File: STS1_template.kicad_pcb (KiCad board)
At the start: 4 copper layers, 85 x 85 mm, 24 parts, among them CON1 DISCO-CON1, CON11 DISCO-CON1, CON2 DISCO-CON2, CON21 DISCO-CON2, IC1 W25Q01JVZEIQ, IC2 CY15B108QN-40SXI, IC3 STM32F411RET6TR, J1 Conn_01x02_Female, J2 Conn_02x16_Odd_Even, J3 Conn_01x02_Female, J4 Conn_02x16_Odd_Even, J5 Conn_02x16_Odd_Even, J6 Conn_02x16_Odd_Even, U1 coordinate_system

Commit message: new template
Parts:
- removed IC3: STM32F411RET6TR, STM32F411RET6TR:QFP50P1200X1200X160-64N
- added C1: 20p, Capacitor_SMD:C_0805_2012Metric, F.Cu at (236.4, 93.4)
- added C10: 100n, Capacitor_SMD:C_0805_2012Metric, F.Cu at (240.9, 93.4)
- added C11: 100n, Capacitor_SMD:C_0805_2012Metric, F.Cu at (209.6, 109.2)
- added C12: 47u, Capacitor_SMD:C_0805_2012Metric, F.Cu at (223.0, 103.7)
- added C13: 100n, Capacitor_SMD:C_0805_2012Metric, F.Cu at (281.3, 76.1)
- added C14: 47u, Capacitor_SMD:C_0805_2012Metric, F.Cu at (276.8, 79.1)
- added C15: 100n, Capacitor_SMD:C_0805_2012Metric, F.Cu at (276.8, 76.1)
- added C16: 47u, Capacitor_SMD:C_0805_2012Metric, F.Cu at (281.3, 79.1)
- added C2: 20p, Capacitor_SMD:C_0805_2012Metric, F.Cu at (263.2, 60.8)
- added C3: 1u, Capacitor_SMD:C_0805_2012Metric, F.Cu at (250.9, 84.1)
- added C4: 100n, Capacitor_SMD:C_0805_2012Metric, F.Cu at (268.8, 69.9)
- added C5: 100n, Capacitor_SMD:C_0805_2012Metric, F.Cu at (264.3, 72.9)
- added C6: 4.7u, Capacitor_SMD:C_0805_2012Metric, F.Cu at (267.7, 66.9)
- added C7: 100n, Capacitor_SMD:C_0805_2012Metric, F.Cu at (264.3, 69.9)
- added C8: 4.7u, Capacitor_SMD:C_0805_2012Metric, F.Cu at (263.2, 66.9)
- added C9: 100n, Capacitor_SMD:C_0805_2012Metric, F.Cu at (267.7, 63.8)
- added D1: LED, LED_SMD:LED_0805_2012Metric, F.Cu at (267.7, 60.8)
- added D2: LED, LED_SMD:LED_0805_2012Metric, F.Cu at (263.2, 63.8)
- added D3: LED, LED_SMD:LED_0805_2012Metric, F.Cu at (214.1, 109.2)
- added FLASH1: W25Q01JVZEIQ, W25Q01JVZEIQ:SON127P800X600X80-9N-D, F.Cu at (180.9, 64.8)
- added FRAM1: CY15B108QN-40SXI, CY15B108QN-40SXI:SOIC127P800X203-8N, F.Cu at (180.9, 56.8)
- added J10: Conn_01x01_Male, Connector_PinHeader_2.54mm:PinHeader_1x01_P2.54mm_Vertical, F.Cu at (237.6, 84.9)
- added J11: Conn_01x01_Male, Connector_PinHeader_2.54mm:PinHeader_1x01_P2.54mm_Vertical, F.Cu at (251.0, 70.9)
- added J12: Conn_01x01_Male, Connector_PinHeader_2.54mm:PinHeader_1x01_P2.54mm_Vertical, F.Cu at (249.9, 89.5)
- added J13: Conn_01x01_Male, Connector_PinHeader_2.54mm:PinHeader_1x01_P2.54mm_Vertical, F.Cu at (251.0, 80.2)
- added J14: Conn_01x01_Male, Connector_PinHeader_2.54mm:PinHeader_1x01_P2.54mm_Vertical, F.Cu at (237.6, 70.9)
- added J15: Conn_01x01_Male, Connector_PinHeader_2.54mm:PinHeader_1x01_P2.54mm_Vertical, F.Cu at (223.1, 66.3)
- added J16: Conn_01x01_Male, Connector_PinHeader_2.54mm:PinHeader_1x01_P2.54mm_Vertical, F.Cu at (224.2, 84.9)
- added J17: Conn_01x01_Male, Connector_PinHeader_2.54mm:PinHeader_1x01_P2.54mm_Vertical, F.Cu at (223.1, 90.9)
- added J18: Conn_01x01_Male, Connector_PinHeader_2.54mm:PinHeader_1x01_P2.54mm_Vertical, F.Cu at (236.5, 66.3)
- added J19: Conn_01x01_Male, Connector_PinHeader_2.54mm:PinHeader_1x01_P2.54mm_Vertical, F.Cu at (224.2, 80.2)
- added J20: Conn_01x01_Male, Connector_PinHeader_2.54mm:PinHeader_1x01_P2.54mm_Vertical, F.Cu at (224.2, 75.6)
- added J21: Conn_01x01_Male, Connector_PinHeader_2.54mm:PinHeader_1x01_P2.54mm_Vertical, F.Cu at (224.2, 70.9)
- added J22: Conn_01x01_Male, Connector_PinHeader_2.54mm:PinHeader_1x01_P2.54mm_Vertical, F.Cu at (223.1, 61.6)
- added J23: Conn_01x01_Male, Connector_PinHeader_2.54mm:PinHeader_1x01_P2.54mm_Vertical, F.Cu at (236.5, 61.6)
- added J24: Conn_01x01_Male, Connector_PinHeader_2.54mm:PinHeader_1x01_P2.54mm_Vertical, F.Cu at (209.7, 105.4)
- added J25: Conn_01x01_Male, Connector_PinHeader_2.54mm:PinHeader_1x01_P2.54mm_Vertical, F.Cu at (209.7, 100.7)
- added J7: Conn_01x01_Male, Connector_PinHeader_2.54mm:PinHeader_1x01_P2.54mm_Vertical, F.Cu at (237.6, 80.2)
- added J8: Conn_01x01_Male, Connector_PinHeader_2.54mm:PinHeader_1x01_P2.54mm_Vertical, F.Cu at (236.5, 89.5)
- added J9: Conn_01x01_Male, Connector_PinHeader_2.54mm:PinHeader_1x01_P2.54mm_Vertical, F.Cu at (251.0, 75.6)
- added R1: 220, Resistor_SMD:R_0805_2012Metric, F.Cu at (249.7, 93.3)
- added R2: 100, Resistor_SMD:R_0805_2012Metric, F.Cu at (264.3, 75.9)
- added R3: 100, Resistor_SMD:R_0805_2012Metric, F.Cu at (245.3, 93.3)
- added R4: 4k7, Resistor_SMD:R_0805_2012Metric, F.Cu at (227.7, 99.9)
- added R5: 100, Resistor_SMD:R_0805_2012Metric, F.Cu at (223.0, 106.7)
- IC1: value W25Q01JVZEIQ -> STM32F411RET6TR; footprint W25Q01JVZEIQ:SON127P800X600X80-9N-D -> STM32F411RET6TR:QFP50P1200X1200X160-64N
- IC2: value CY15B108QN-40SXI -> STWD100PYW83F; footprint CY15B108QN-40SXI:SOIC127P800X203-8N -> SamacSys_Parts:SOT65P210X110-5N
- J1: footprint Connector_PinSocket_2.00mm:PinSocket_1x02_P2.00mm_Vertical -> Connector_PinHeader_2.54mm:PinHeader_1x02_P2.54mm_Vertical
- J2: value Conn_02x16_Odd_Even -> Conn_01x05_Female; footprint Connector_PinHeader_2.00mm:PinHeader_2x16_P2.00mm_Vertical_SMD -> Connector_PinHeader_2.54mm:PinHeader_1x05_P2.54mm_Horizontal
- J3: value Conn_01x02_Female -> Conn_01x01_Male; footprint Connector_PinSocket_2.00mm:PinSocket_1x02_P2.00mm_Vertical -> Connector_PinHeader_2.54mm:PinHeader_1x01_P2.54mm_Vertical
- J4, J5, J6: value Conn_02x16_Odd_Even -> Conn_01x01_Male; footprint Connector_PinHeader_2.00mm:PinHeader_2x16_P2.00mm_Vertical_SMD -> Connector_PinHeader_2.54mm:PinHeader_1x01_P2.54mm_Vertical
- moved J3 92.9 mm to (209.7, 90.9)
- moved J4 91.8 mm to (249.9, 61.6), turned to 0 degrees
- moved J5 86.4 mm to (237.6, 75.6), turned to 0 degrees
- moved IC2 67.8 mm to (223.1, 100.3), turned to 0 degrees
- moved J6 67.7 mm to (249.9, 66.3)
- moved J1 67.6 mm to (236.0, 100.3)
- moved J2 43.0 mm to (152.9, 43.8), turned to 90 degrees
- moved IC1 30.6 mm to (156.9, 83.8), turned to 0 degrees
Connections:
- net Earth renamed Net-(IC1-Pad4)
- IC1 pad 1: Net-(IC1-Pad1) -> /STS1_RF/LoRa_VCC
- IC1 pad 5: Net-(IC1-Pad5) -> Net-(C1-Pad2)
- IC1 pad 7: Net-(IC1-Pad7) -> /STS1_COBC_uC/STM32_NRST
- IC1 pad 8: +3V3 -> Net-(IC1-Pad8)
- IC2 pad 2: Net-(IC2-Pad2) -> GND
- IC2 pad 3: Net-(IC2-Pad3) -> GND
- IC2 pad 4: Net-(IC2-Pad4) -> /STS1_COBC_uC/STM32_PA9(Watchdog_toggle)
- IC2 pad 5: Net-(IC2-Pad5) -> /STS1_RF/LoRa_VCC
- J1 pad 1: Net-(J1-Pad1) -> GND
- J1 pad 2: Net-(J1-Pad2) -> /STS1_RF/LoRa_VCC
- J2 pad 1: Net-(J2-Pad1) -> /STS1_RF/LoRa_VCC
- J2 pad 2: Net-(IC3-Pad1) -> Net-(IC1-Pad49)
- J2 pad 3: Net-(J2-Pad3) -> GND
- J2 pad 4: Net-(IC3-Pad2) -> Net-(IC1-Pad46)
- J2 pad 5: Net-(J2-Pad5) -> /STS1_COBC_uC/STM32_NRST
- J3 pad 1: Net-(J3-Pad1) -> /STS1_RF/LoRa_NSS
- J4 pad 1: Net-(IC3-Pad64) -> /STS1_RF/RF4463_SDI
- J5 pad 1: Net-(J5-Pad1) -> /STS1_COBC_Memories/FRAM_DataOutput
- J6 pad 1: Net-(IC3-Pad48) -> /STS1_COBC_Memories/FRAM_DataInput
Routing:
- net Net-(IC1-Pad6): track 115.8 -> 0.00 mm
- net +3V3: track 86.2 -> 0.00 mm, vias 4 -> 5
- net Net-(IC2-Pad2): track 49.0 -> 0.00 mm
- net Net-(IC3-Pad17): track 23.4 -> 0.00 mm
- net Net-(IC3-Pad33): track 23.2 -> 0.00 mm
- net Net-(IC3-Pad32): track 23.2 -> 0.00 mm
- net Net-(IC3-Pad48): track 22.9 -> 0.00 mm
- net Net-(IC3-Pad35): track 22.8 -> 0.00 mm
- net Net-(IC3-Pad18): track 22.7 -> 0.00 mm
- net Net-(IC3-Pad34): track 22.6 -> 0.00 mm
- net Net-(IC3-Pad31): track 22.6 -> 0.00 mm
- net Net-(IC3-Pad47): track 22.4 -> 0.00 mm
- net Net-(IC3-Pad19): track 22.1 -> 0.00 mm
- net Net-(IC3-Pad30): track 22.0 -> 0.00 mm
- net Net-(IC3-Pad46): track 21.6 -> 0.00 mm
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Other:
- board text added: "TU Wien Space Team STS [STS1 COBC Prototype] v1.0"
- board text removed: "TU Wien Space Team STS1 [COBC] [V1]"

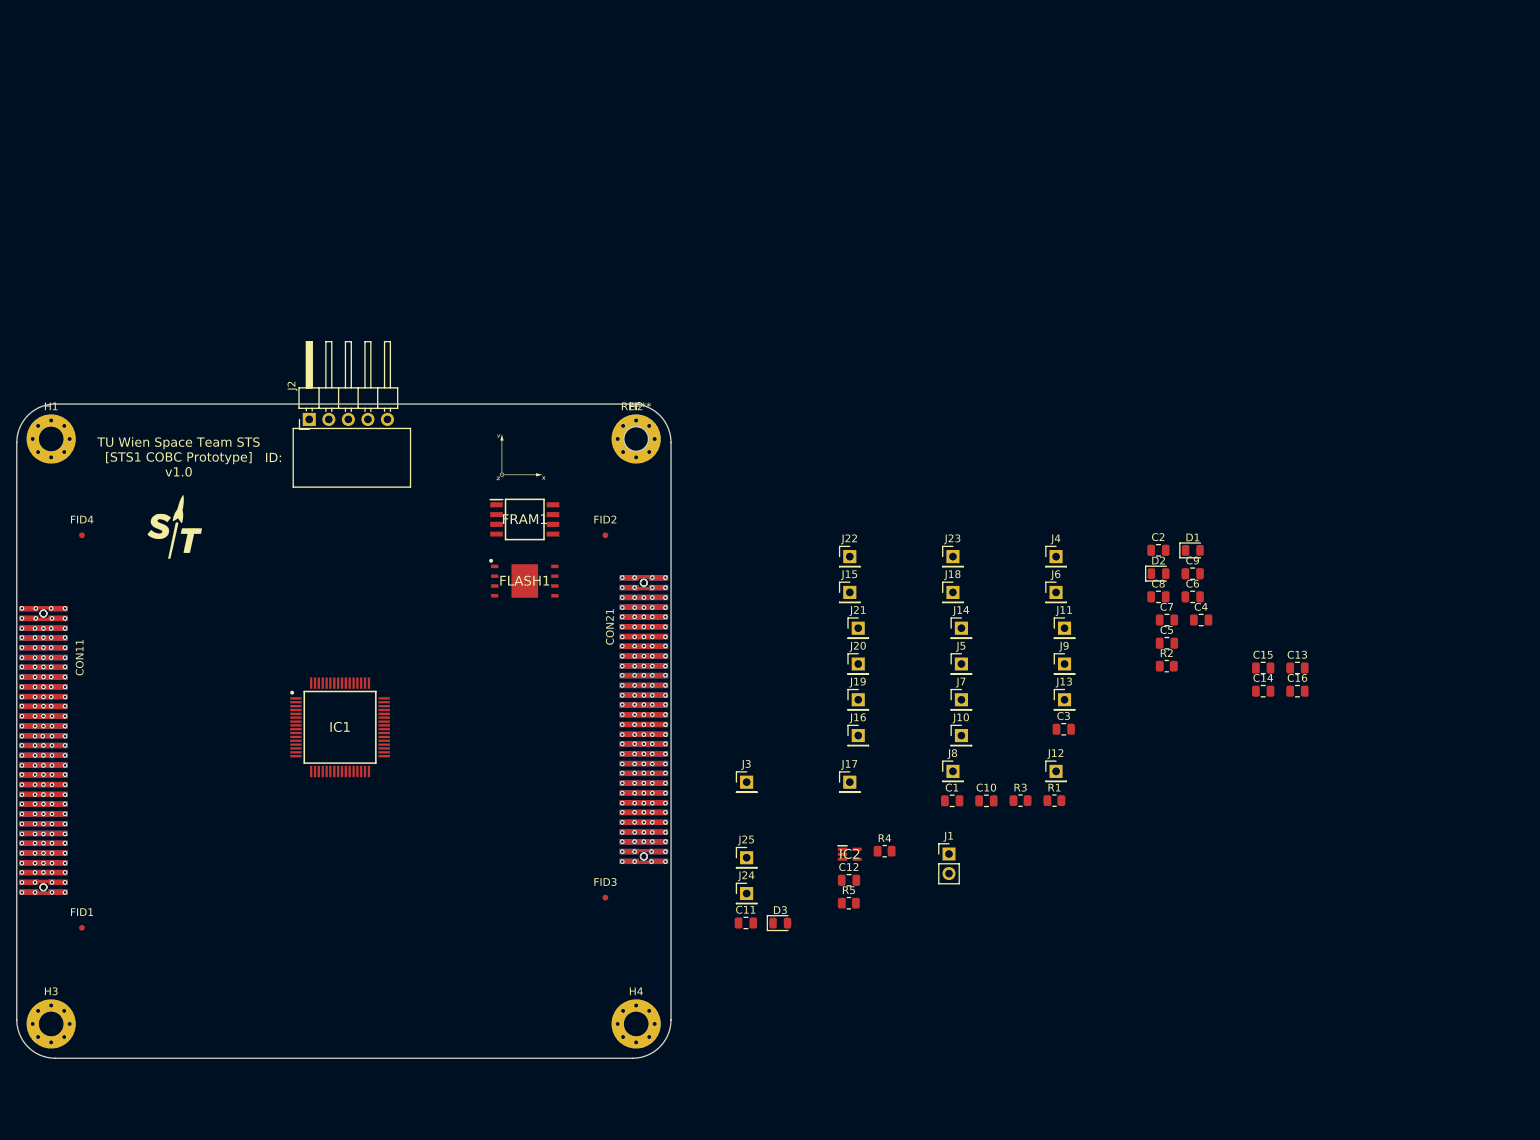
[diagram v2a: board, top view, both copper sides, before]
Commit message: Issues removed + further layout development
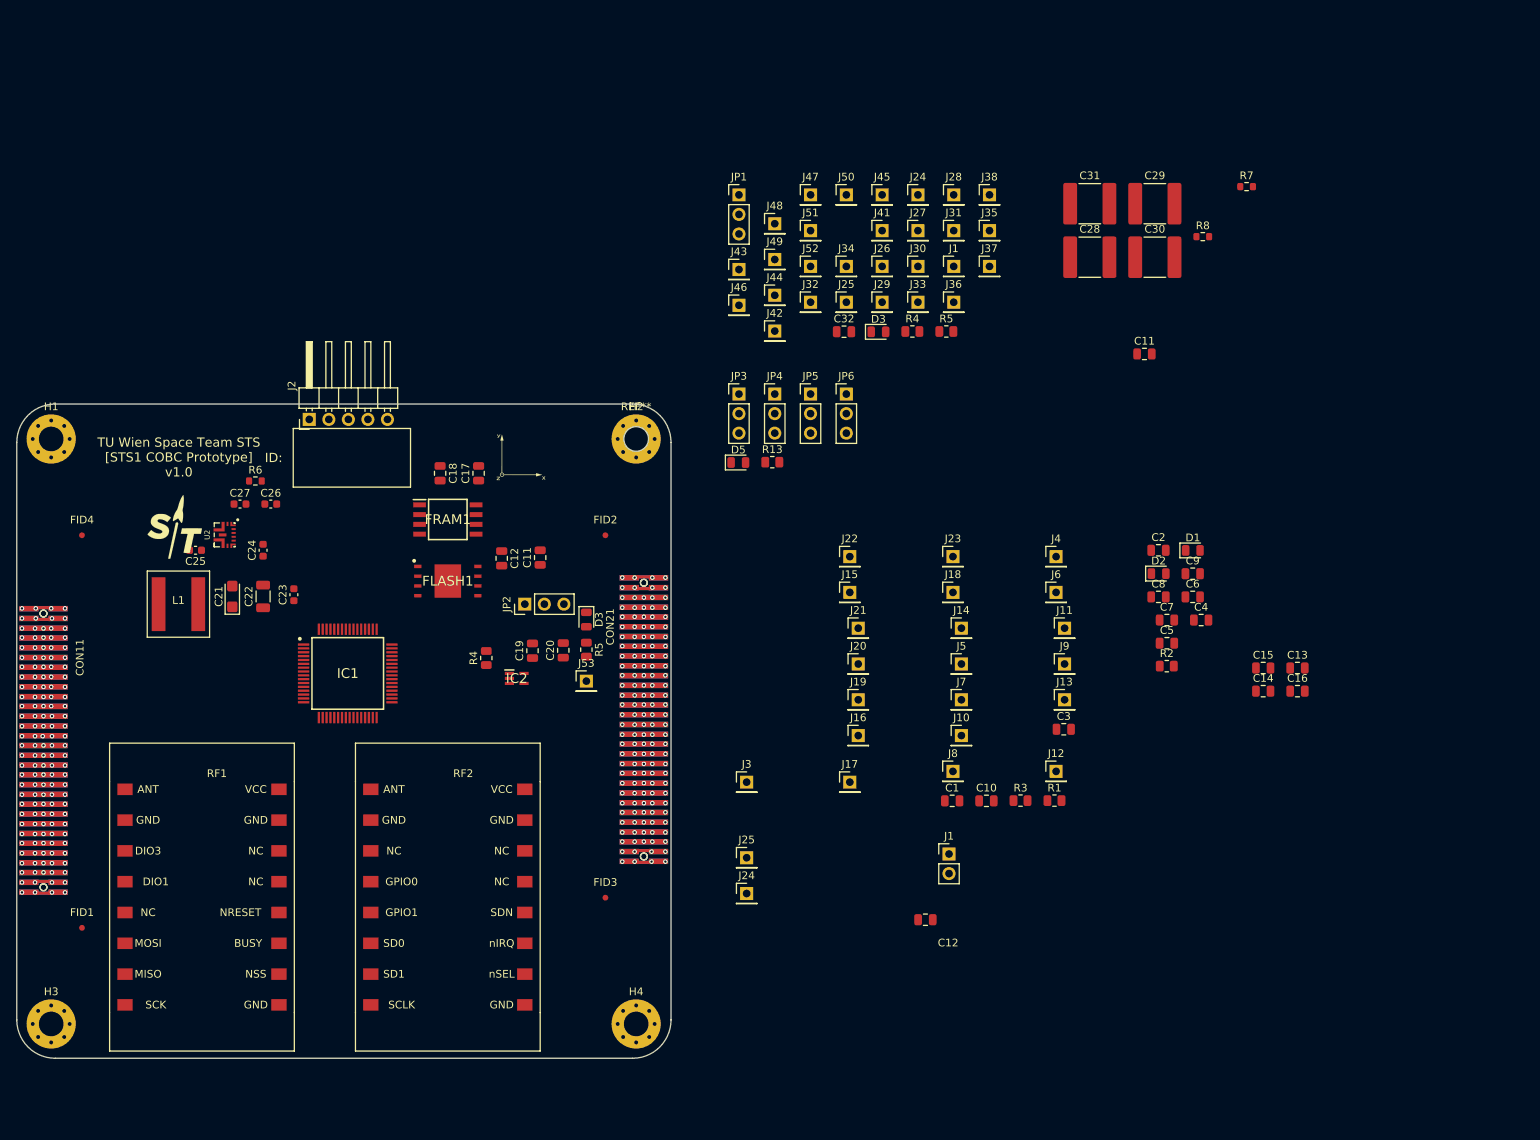
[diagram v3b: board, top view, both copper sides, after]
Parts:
- added C11: 100n, Capacitor_SMD:C_0805_2012Metric, F.Cu at (261.4, 35.3)
- added C12: 47u, Capacitor_SMD:C_0805_2012Metric, F.Cu at (177.9, 61.9)
- added C17: 100n, Capacitor_SMD:C_0805_2012Metric, F.Cu at (174.9, 50.8)
- added C18: 47u, Capacitor_SMD:C_0805_2012Metric, F.Cu at (169.9, 50.8)
- added C19: 100n, Capacitor_SMD:C_0805_2012Metric, F.Cu at (181.9, 73.8)
- added C20: 47u, Capacitor_SMD:C_0805_2012Metric, F.Cu at (185.9, 73.8)
- added C21: 47uF, Capacitor_Tantalum_SMD:CP_EIA-3216-18_Kemet-A, F.Cu at (142.9, 66.8)
- added C22: 10uF, Capacitor_SMD:C_1206_3216Metric, F.Cu at (146.9, 66.8)
- added C23: 100nF, Capacitor_SMD:C_0603_1608Metric, F.Cu at (150.9, 66.6)
- added C24: 150nF, Capacitor_SMD:C_0603_1608Metric, F.Cu at (146.9, 60.8)
- added C25: 2.2uF, Capacitor_SMD:C_0603_1608Metric, F.Cu at (138.1, 60.8)
- added C26: 39nF, Capacitor_SMD:C_0603_1608Metric, F.Cu at (147.9, 54.8)
- added C27: 82pF, Capacitor_SMD:C_0603_1608Metric, F.Cu at (143.9, 54.8)
- added C28: 68uF, Capacitor_SMD:C_2220_5650Metric, F.Cu at (254.3, 22.7)
- added C29: 68uF, Capacitor_SMD:C_2220_5650Metric, F.Cu at (262.8, 15.8)
- added C30: 68uF, Capacitor_SMD:C_2220_5650Metric, F.Cu at (262.8, 22.7)
- added C31: 68uF, Capacitor_SMD:C_2220_5650Metric, F.Cu at (254.3, 15.8)
- added C32: 100n, Capacitor_SMD:C_0805_2012Metric, F.Cu at (222.4, 32.4)
- added D3: LED, LED_SMD:LED_0805_2012Metric, F.Cu at (226.8, 32.4)
- added D5: LED, LED_SMD:LED_0805_2012Metric, F.Cu at (208.6, 49.4)
- added J1: Conn_01x01_Male, Connector_PinHeader_2.54mm:PinHeader_1x01_P2.54mm_Vertical, F.Cu at (236.6, 23.9)
- added J24: Conn_01x01_Male, Connector_PinHeader_2.54mm:PinHeader_1x01_P2.54mm_Vertical, F.Cu at (232.0, 14.6)
- added J25: Conn_01x01_Male, Connector_PinHeader_2.54mm:PinHeader_1x01_P2.54mm_Vertical, F.Cu at (222.7, 28.6)
- added J26: Conn_01x01_Male, Connector_PinHeader_2.54mm:PinHeader_1x01_P2.54mm_Vertical, F.Cu at (227.3, 23.9)
- added J27: Conn_01x01_Male, Connector_PinHeader_2.54mm:PinHeader_1x01_P2.54mm_Vertical, F.Cu at (232.0, 19.3)
- added J28: Conn_01x01_Male, Connector_PinHeader_2.54mm:PinHeader_1x01_P2.54mm_Vertical, F.Cu at (236.6, 14.6)
- added J29: Conn_01x01_Male, Connector_PinHeader_2.54mm:PinHeader_1x01_P2.54mm_Vertical, F.Cu at (227.3, 28.6)
- added J30: Conn_01x01_Male, Connector_PinHeader_2.54mm:PinHeader_1x01_P2.54mm_Vertical, F.Cu at (232.0, 23.9)
- added J31: Conn_01x01_Male, Connector_PinHeader_2.54mm:PinHeader_1x01_P2.54mm_Vertical, F.Cu at (236.6, 19.3)
- added J32: Conn_01x01_Male, Connector_PinHeader_2.54mm:PinHeader_1x01_P2.54mm_Vertical, F.Cu at (218.0, 28.6)
- added J33: Conn_01x01_Male, Connector_PinHeader_2.54mm:PinHeader_1x01_P2.54mm_Vertical, F.Cu at (232.0, 28.6)
- added J34: Conn_01x01_Male, Connector_PinHeader_2.54mm:PinHeader_1x01_P2.54mm_Vertical, F.Cu at (222.7, 23.9)
- added J35: Conn_01x01_Male, Connector_PinHeader_2.54mm:PinHeader_1x01_P2.54mm_Vertical, F.Cu at (241.3, 19.3)
- added J36: Conn_01x01_Male, Connector_PinHeader_2.54mm:PinHeader_1x01_P2.54mm_Vertical, F.Cu at (236.6, 28.6)
- added J37: Conn_01x01_Male, Connector_PinHeader_2.54mm:PinHeader_1x01_P2.54mm_Vertical, F.Cu at (241.3, 23.9)
- added J38: Conn_01x01_Male, Connector_PinHeader_2.54mm:PinHeader_1x01_P2.54mm_Vertical, F.Cu at (241.3, 14.6)
- added J41: Conn_01x01_Male, Connector_PinHeader_2.54mm:PinHeader_1x01_P2.54mm_Vertical, F.Cu at (227.3, 19.3)
- added J42: Conn_01x01_Male, Connector_PinHeader_2.54mm:PinHeader_1x01_P2.54mm_Vertical, F.Cu at (213.4, 32.3)
- added J43: Conn_01x01_Male, Connector_PinHeader_2.54mm:PinHeader_1x01_P2.54mm_Vertical, F.Cu at (208.7, 24.3)
- added J44: Conn_01x01_Male, Connector_PinHeader_2.54mm:PinHeader_1x01_P2.54mm_Vertical, F.Cu at (213.4, 27.7)
- added J45: Conn_01x01_Male, Connector_PinHeader_2.54mm:PinHeader_1x01_P2.54mm_Vertical, F.Cu at (227.3, 14.6)
- added J46: Conn_01x01_Male, Connector_PinHeader_2.54mm:PinHeader_1x01_P2.54mm_Vertical, F.Cu at (208.7, 29.0)
- added J47: Conn_01x01_Male, Connector_PinHeader_2.54mm:PinHeader_1x01_P2.54mm_Vertical, F.Cu at (218.0, 14.6)
- added J48: Conn_01x01_Male, Connector_PinHeader_2.54mm:PinHeader_1x01_P2.54mm_Vertical, F.Cu at (213.4, 18.4)
- added J49: Conn_01x01_Male, Connector_PinHeader_2.54mm:PinHeader_1x01_P2.54mm_Vertical, F.Cu at (213.4, 23.0)
- added J50: Conn_01x01_Male, Connector_PinHeader_2.54mm:PinHeader_1x01_P2.54mm_Vertical, F.Cu at (222.7, 14.6)
- added J51: Conn_01x01_Male, Connector_PinHeader_2.54mm:PinHeader_1x01_P2.54mm_Vertical, F.Cu at (218.0, 19.3)
- added J52: Conn_01x01_Male, Connector_PinHeader_2.54mm:PinHeader_1x01_P2.54mm_Vertical, F.Cu at (218.0, 23.9)
- added J53: Conn_01x01_Male, Connector_PinHeader_2.54mm:PinHeader_1x01_P2.54mm_Vertical, F.Cu at (188.9, 77.8)
- added JP1: Jumper_NC_Dual, Connector_PinHeader_2.54mm:PinHeader_1x03_P2.54mm_Vertical, F.Cu at (208.7, 14.6)
- added JP2: Jumper_NC_Dual, Connector_PinHeader_2.54mm:PinHeader_1x03_P2.54mm_Vertical, F.Cu at (180.9, 67.8)
- added JP3: Jumper_NC_Dual, Connector_PinHeader_2.54mm:PinHeader_1x03_P2.54mm_Vertical, F.Cu at (208.7, 40.5)
- added JP4: Jumper_NC_Dual, Connector_PinHeader_2.54mm:PinHeader_1x03_P2.54mm_Vertical, F.Cu at (213.4, 40.5)
- added JP5: Jumper_NC_Dual, Connector_PinHeader_2.54mm:PinHeader_1x03_P2.54mm_Vertical, F.Cu at (218.0, 40.5)
- added JP6: Jumper_NC_Dual, Connector_PinHeader_2.54mm:PinHeader_1x03_P2.54mm_Vertical, F.Cu at (222.7, 40.5)
- added L1: 1uH, STS1_DCDC:XAL8080, F.Cu at (135.9, 67.8)
- added R13: 15, Resistor_SMD:R_0805_2012Metric, F.Cu at (213.1, 49.4)
- added R4: 4k7, Resistor_SMD:R_0805_2012Metric, F.Cu at (231.3, 32.4)
- added R5: 100, Resistor_SMD:R_0805_2012Metric, F.Cu at (235.7, 32.4)
- added R6: 48k7, Resistor_SMD:R_0603_1608Metric, F.Cu at (145.9, 51.8)
- added R7: 357k, Resistor_SMD:R_0603_1608Metric, F.Cu at (274.7, 13.6)
- added R8: 48k7, Resistor_SMD:R_0603_1608Metric, F.Cu at (269.0, 20.1)
- added RF1: LoRa1268F30, STS1_RF:LoRa1268F30, F.Cu at (149.0, 91.9)
- added RF2: RF4463F30, STS1_RF:STS1_RF4463F30, F.Cu at (180.9, 91.9)
- added U2: TPS61288, STS1_DCDC:VQFN-HR, F.Cu at (141.9, 58.8)
- moved R4 57.5 mm to (175.9, 74.8), turned to 90 degrees
- moved C11 54.5 mm to (182.9, 61.8), turned to 90 degrees
- moved IC2 48.9 mm to (179.8, 77.5)
- moved R5 47.4 mm to (188.9, 73.7), turned to 270 degrees
- moved D3 46.8 mm to (188.9, 69.8), turned to 270 degrees
- moved C12 11.2 mm to (232.9, 108.8)
- moved FLASH1 10.0 mm to (170.9, 64.8)
- moved FRAM1 10.0 mm to (170.9, 56.8)
- moved IC1 7.07 mm to (157.9, 76.8)
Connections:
- C10 pad 1: /STS1_RF/LoRa_VCC -> +3V3
- C13 pad 1: /STS1_RF/LoRa_VCC -> +5V
- C14 pad 1: /STS1_RF/LoRa_VCC -> +5V
- C15 pad 1: /STS1_RF/LoRa_VCC -> +5V
- C16 pad 1: /STS1_RF/LoRa_VCC -> +5V
- C3 pad 1: Net-(C3-Pad1) -> +3V3
- C4 pad 2: Net-(C3-Pad1) -> +3V3
- C5 pad 2: /STS1_RF/LoRa_VCC -> +3V3
- C6 pad 2: /STS1_RF/LoRa_VCC -> +3V3
- C7 pad 2: /STS1_RF/LoRa_VCC -> +3V3
- C9 pad 1: /STS1_RF/LoRa_VCC -> +3V3
- FLASH1 pad 3: Net-(FLASH1-Pad3) -> /STS1_COBC_Memories/Flash_WP
- FLASH1 pad 7: /STS1_COBC_Memories/Flash_PowerSupply -> Net-(FLASH1-Pad7)
- FLASH1 pad 8: /STS1_COBC_Memories/Flash_PowerSupply -> +3V3
- FRAM1 pad 1: GND -> /STS1_COBC_Memories/FRAM_CS
- FRAM1 pad 3: GND -> +3V3
- FRAM1 pad 4: /STS1_COBC_Memories/FRAM_PowerSupply -> GND
- FRAM1 pad 7: GND -> +3V3
- FRAM1 pad 8: GND -> +3V3
- IC1 pad 1: /STS1_RF/LoRa_VCC -> +3V3
- IC1 pad 13: Net-(C3-Pad1) -> +3V3
- IC1 pad 19: /STS1_RF/LoRa_VCC -> +3V3
- IC1 pad 2: Net-(IC1-Pad2) -> /STS1_COBC_uC/PC13
- IC1 pad 24: Net-(IC1-Pad24) -> /STS1_COBC_Memories/Flash_WP
- IC1 pad 28: Net-(IC1-Pad28) -> GND
- IC1 pad 3: Net-(IC1-Pad3) -> /STS1_COBC_uC/PC14
- IC1 pad 32: /STS1_RF/LoRa_VCC -> +3V3
- IC1 pad 4: Net-(IC1-Pad4) -> /STS1_COBC_uC/PC15
- IC1 pad 48: /STS1_RF/LoRa_VCC -> +3V3
- IC1 pad 50: Net-(IC1-Pad50) -> /STS1_COBC_uC/PA15
- IC1 pad 54: Net-(IC1-Pad54) -> /STS1_COBC_uC/PD2
- IC1 pad 55: Net-(IC1-Pad55) -> /STS1_COBC_uC/PB3
- IC1 pad 56: Net-(IC1-Pad56) -> /STS1_COBC_uC/PB4
- IC1 pad 57: Net-(IC1-Pad57) -> /STS1_COBC_uC/PB5
- IC1 pad 58: Net-(IC1-Pad58) -> /STS1_COBC_uC/PB6
- IC1 pad 59: Net-(IC1-Pad59) -> /STS1_COBC_uC/PB7
- IC1 pad 60: GND -> Net-(IC1-Pad60)
- IC1 pad 61: Net-(IC1-Pad61) -> /STS1_COBC_uC/PB9
- IC1 pad 62: /STS1_COBC_uC/SPI2_NSS -> /STS1_COBC_Memories/FRAM_CS
- IC1 pad 64: /STS1_RF/LoRa_VCC -> +3V3
- IC1 pad 8: Net-(IC1-Pad8) -> /STS1_COBC_uC/PC0
- IC1 pad 9: Net-(IC1-Pad9) -> /STS1_COBC_uC/PC1
- IC2 pad 5: /STS1_RF/LoRa_VCC -> +3V3
- J11 pad 1: /STS1_COBC_uC/SPI2_NSS -> /STS1_COBC_Memories/FRAM_CS
- J16 pad 1: /STS1_RF/LoRa_VCC -> +3V3
- J18 pad 1: /STS1_RF/LoRa_VCC -> +3V3
- J2 pad 1: /STS1_RF/LoRa_VCC -> +3V3
- J7 pad 1: /STS1_RF/LoRa_VCC -> +3V3
- J8 pad 1: /STS1_RF/LoRa_VCC -> +3V3
